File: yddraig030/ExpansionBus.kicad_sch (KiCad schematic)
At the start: 11 parts

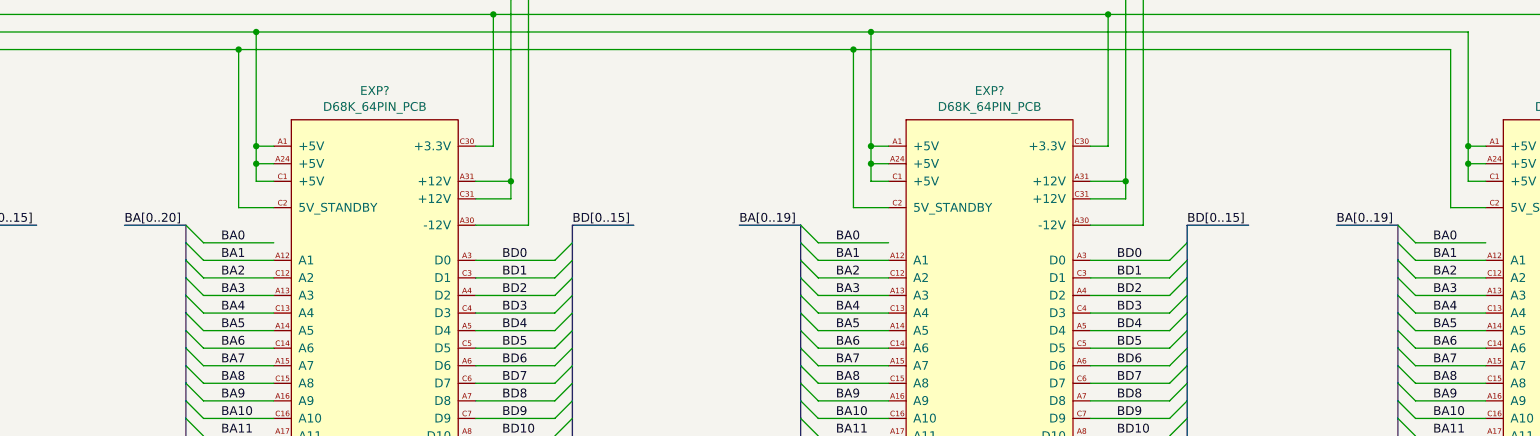
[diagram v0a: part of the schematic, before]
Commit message: yddraig030: some small changes to the schematic
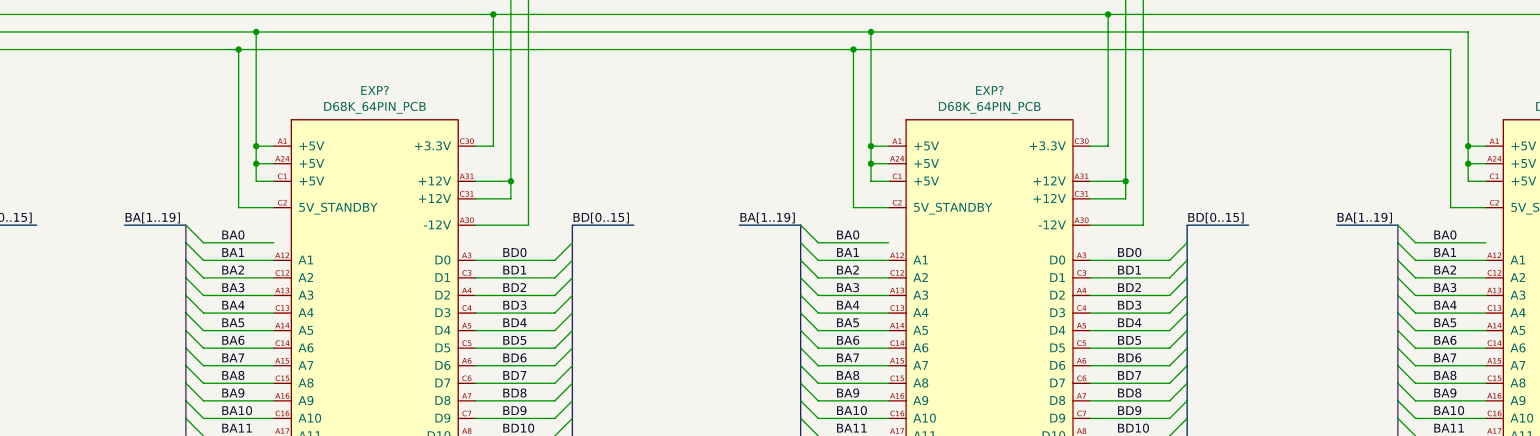
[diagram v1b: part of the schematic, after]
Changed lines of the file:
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@@
     (effects (font (size 1.27 1.27)) (justify left bottom))
   )
-  (label "BA[0..19]" (at 227.33 72.39 0)
+  (label "BA[1..19]" (at 227.33 72.39 0)
     (effects (font (size 1.27 1.27)) (justify left bottom))
   )
@@
     (effects (font (size 1.27 1.27)) (justify left bottom))
   )
-  (label "BA[0..20]" (at 138.43 72.39 0)
+  (label "BA[1..19]" (at 138.43 72.39 0)
     (effects (font (size 1.27 1.27)) (justify left bottom))
   )
@@
     (effects (font (size 1.27 1.27)) (justify left bottom))
   )
-  (label "BA[0..19]" (at 313.69 72.39 0)
+  (label "BA[1..19]" (at 313.69 72.39 0)
     (effects (font (size 1.27 1.27)) (justify left bottom))
   )
@@
     (pin "1")
   )
-  (symbol (lib_id "Device:C") (at 170.18 255.27 0)
+  (symbol (lib_id "Device:C") (at 170.18 255.27 0) (unit 1)
     (in_bom yes) (on_board yes)
     (property "Reference" "C?" (id 0) (at 173.101 254.1016 0)
@@
     (pin "2")
   )
-  (symbol (lib_id "power:GND") (at 170.18 264.16 0)
+  (symbol (lib_id "power:GND") (at 170.18 264.16 0) (unit 1)
     (in_bom yes) (on_board yes)
     (property "Reference" "#PWR?" (id 0) (at 170.18 270.51 0)
@@
     (pin "1")
   )
-  (symbol (lib_id "Device:C") (at 182.88 255.27 0)
+  (symbol (lib_id "Device:C") (at 182.88 255.27 0) (unit 1)
     (in_bom yes) (on_board yes)
     (property "Reference" "C?" (id 0) (at 185.801 254.1016 0)
@@
     (pin "2")
   )
-  (symbol (lib_id "power:+5V") (at 170.18 246.38 0)
+  (symbol (lib_id "power:+5V") (at 170.18 246.38 0) (unit 1)
     (in_bom yes) (on_board yes)
     (property "Reference" "#PWR?" (id 0) (at 170.18 250.19 0)
@@
     (pin "7")
   )
-  (symbol (lib_id "Ddraig:D68K_64PIN_PCB") (at 175.26 105.41 0)
+  (symbol (lib_id "Ddraig:D68K_64PIN_PCB") (at 175.26 105.41 0) (unit 1)
     (in_bom yes) (on_board yes)
     (property "Reference" "EXP?" (id 0) (at 174.625 52.959 0))
@@
     (pin "C9")
   )
-  (symbol (lib_id "Ddraig:D68K_64PIN_PCB") (at 264.16 105.41 0)
+  (symbol (lib_id "Ddraig:D68K_64PIN_PCB") (at 264.16 105.41 0) (unit 1)
     (in_bom yes) (on_board yes)
     (property "Reference" "EXP?" (id 0) (at 263.525 52.959 0))
@@
     (pin "C9")
   )
-  (symbol (lib_id "Ddraig:D68K_64PIN_PCB") (at 350.52 105.41 0)
+  (symbol (lib_id "Ddraig:D68K_64PIN_PCB") (at 350.52 105.41 0) (unit 1)
     (in_bom yes) (on_board yes)
     (property "Reference" "EXP?" (id 0) (at 349.885 52.959 0))
@@
     (pin "1")
   )
-  (symbol (lib_id "Ddraig:D68K_64PIN_PCB") (at 88.9 105.41 0)
+  (symbol (lib_id "Ddraig:D68K_64PIN_PCB") (at 88.9 105.41 0) (unit 1)
     (in_bom yes) (on_board yes)
     (property "Reference" "EXP?" (id 0) (at 88.265 52.959 0))
